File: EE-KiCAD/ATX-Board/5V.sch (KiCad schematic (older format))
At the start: 23 parts, among them Q101 BSC026N08NS5ATMA1, Q102 BSC026N08NS5ATMA1, Q103 BSC026N08NS5ATMA1, Q104 BSC026N08NS5ATMA1, U102 TPS53015

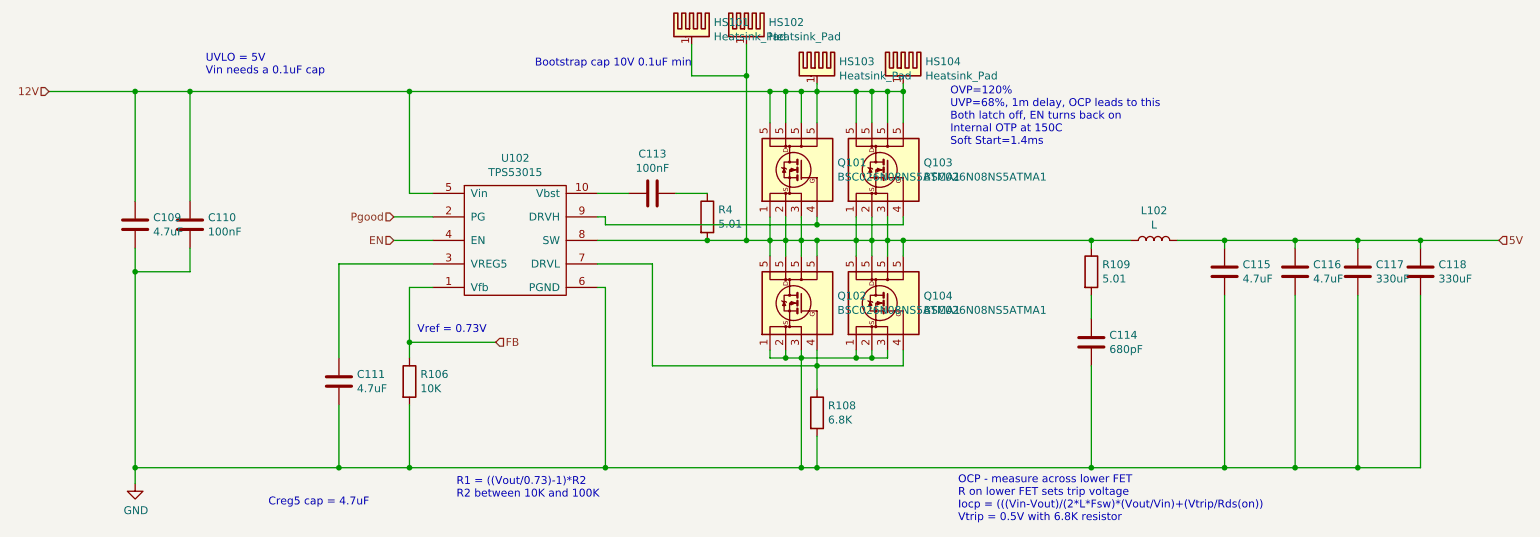
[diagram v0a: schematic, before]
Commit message: Finish first draft of PCBs.  Pulled PCBs into OpenSCAD for fitment.
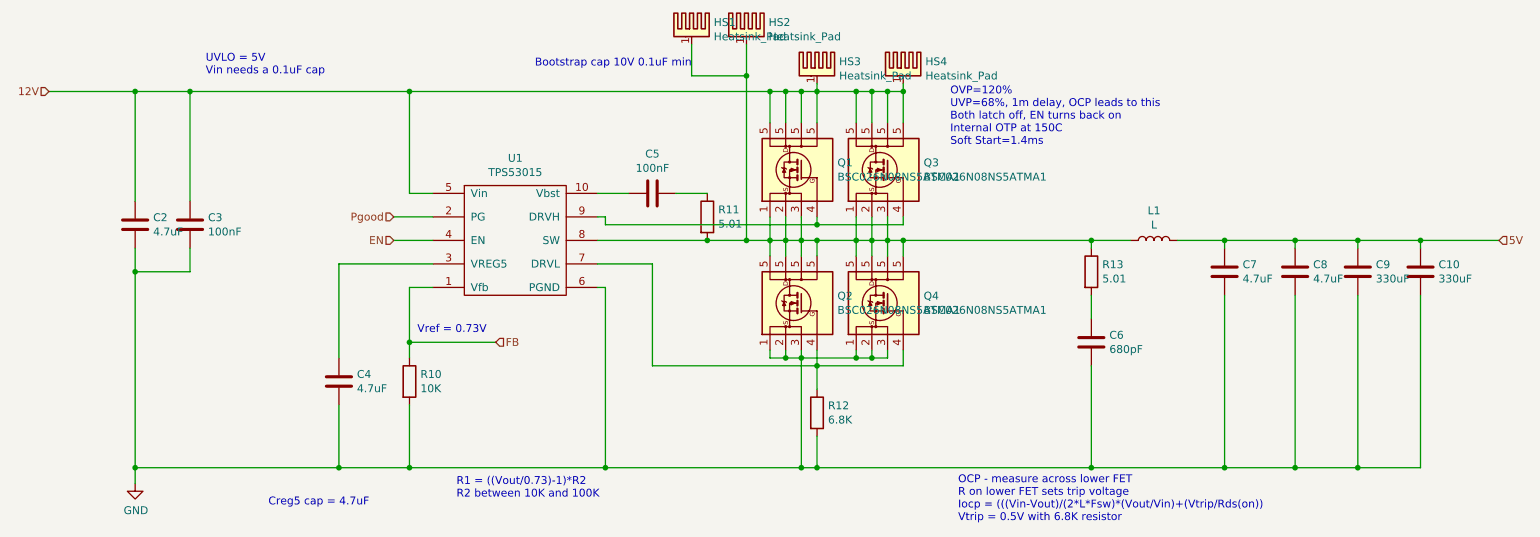
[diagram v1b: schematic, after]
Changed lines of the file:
@@
 $Descr USLedger 17000 11000
 encoding utf-8
-Sheet 6 9
+Sheet 8 8
 Title ""
 Date "2018-08-23"
@@
 AR Path="/5B7F1B83" Ref="U?"  Part="1"
 AR Path="/603813BC/5B7F1B83" Ref="U1"  Part="1"
-F 0 "U102" H 8425 5775 50  0000 C CNN
+F 0 "U1" H 8425 5775 50  0000 C CNN
 F 1 "TPS53015" H 8425 5684 50  0000 C CNN
 F 2 "AEvan:VSSOP-10_2.4x2.1mm_Pitch0.5mm" H 8500 4850 50  0001 C CNN
@@
 AR Path="/5B7EFFE7/5B7F1CF3" Ref="Q101"  Part="1"
 AR Path="/603813BC/5B7F1CF3" Ref="Q1"  Part="1"
-F 0 "Q101" V 10296 4570 50  0000 R CNN
+F 0 "Q1" V 10296 4570 50  0000 R CNN
 F 1 "BSC026N08NS5ATMA1" V 10205 4570 50  0000 R CNN
 F 2 "Package_TO_SOT_SMD:TDSON-8-1" H 10250 5000 50  0001 C CIN
@@
 AR Path="/5B7EFFE7/5B7F1D6B" Ref="Q102"  Part="1"
 AR Path="/603813BC/5B7F1D6B" Ref="Q2"  Part="1"
-F 0 "Q102" V 10296 5420 50  0000 R CNN
+F 0 "Q2" V 10296 5420 50  0000 R CNN
 F 1 "BSC026N08NS5ATMA1" V 10205 5420 50  0000 R CNN
 F 2 "Package_TO_SOT_SMD:TDSON-8-1" H 10250 5850 50  0001 C CIN
@@
 AR Path="/5B7EFFE7/5B7F1E13" Ref="L102"  Part="1"
 AR Path="/603813BC/5B7F1E13" Ref="L1"  Part="1"
-F 0 "L102" V 12690 5250 50  0000 C CNN
+F 0 "L1" V 12690 5250 50  0000 C CNN
 F 1 "L" V 12599 5250 50  0000 C CNN
 F 2 "Inductor_SMD:L_12x12mm_H8mm" H 12500 5250 50  0001 C CNN
@@
 AR Path="/5B7EFFE7/5B7F1F01" Ref="C115"  Part="1"
 AR Path="/603813BC/5B7F1F01" Ref="C7"  Part="1"
-F 0 "C115" H 13065 5496 50  0000 L CNN
+F 0 "C7" H 13065 5496 50  0000 L CNN
 F 1 "4.7uF" H 13065 5405 50  0000 L CNN
 F 2 "AEvan:0805_C" H 12988 5300 50  0001 C CNN
@@
 AR Path="/5B7EFFE7/5B7F1F63" Ref="C116"  Part="1"
 AR Path="/603813BC/5B7F1F63" Ref="C8"  Part="1"
-F 0 "C116" H 13515 5496 50  0000 L CNN
+F 0 "C8" H 13515 5496 50  0000 L CNN
 F 1 "4.7uF" H 13515 5405 50  0000 L CNN
 F 2 "AEvan:0805_C" H 13438 5300 50  0001 C CNN
@@
 AR Path="/5B7EFFE7/5B7F1FA1" Ref="C117"  Part="1"
 AR Path="/603813BC/5B7F1FA1" Ref="C9"  Part="1"
-F 0 "C117" H 13915 5496 50  0000 L CNN
+F 0 "C9" H 13915 5496 50  0000 L CNN
 F 1 "330uF" H 13915 5405 50  0000 L CNN
 F 2 "Capacitor_THT:C_Radial_D6.3mm_H7.0mm_P2.50mm" H 13838 5300 50  0001 C CNN
@@
 AR Path="/5B7EFFE7/5B7F1FD7" Ref="C118"  Part="1"
 AR Path="/603813BC/5B7F1FD7" Ref="C10"  Part="1"
-F 0 "C118" H 14315 5496 50  0000 L CNN
+F 0 "C10" H 14315 5496 50  0000 L CNN
 F 1 "330uF" H 14315 5405 50  0000 L CNN
 F 2 "Capacitor_THT:C_Radial_D6.3mm_H7.0mm_P2.50mm" H 14238 5300 50  0001 C CNN
@@
 AR Path="/5B7EFFE7/5B7F2039" Ref="C113"  Part="1"
 AR Path="/603813BC/5B7F2039" Ref="C5"  Part="1"
-F 0 "C113" V 9048 4950 50  0000 C CNN
+F 0 "C5" V 9048 4950 50  0000 C CNN
 F 1 "100nF" V 9139 4950 50  0000 C CNN
 F 2 "AEvan:0805_C" H 9338 4800 50  0001 C CNN
@@
 AR Path="/5B7EFFE7/5B7F2089" Ref="C114"  Part="1"
 AR Path="/603813BC/5B7F2089" Ref="C6"  Part="1"
-F 0 "C114" H 12215 5946 50  0000 L CNN
+F 0 "C6" H 12215 5946 50  0000 L CNN
 F 1 "680pF" H 12215 5855 50  0000 L CNN
 F 2 "AEvan:0805_C" H 12138 5750 50  0001 C CNN
@@
 AR Path="/5B7EFFE7/5B7F2119" Ref="C111"  Part="1"
 AR Path="/603813BC/5B7F2119" Ref="C4"  Part="1"
-F 0 "C111" H 7415 6196 50  0000 L CNN
+F 0 "C4" H 7415 6196 50  0000 L CNN
 F 1 "4.7uF" H 7415 6105 50  0000 L CNN
 F 2 "AEvan:0805_C" H 7338 6000 50  0001 C CNN
@@
 AR Path="/5B7EFFE7/5B7F2193" Ref="C110"  Part="1"
 AR Path="/603813BC/5B7F2193" Ref="C3"  Part="1"
-F 0 "C110" H 6465 5196 50  0000 L CNN
+F 0 "C3" H 6465 5196 50  0000 L CNN
 F 1 "100nF" H 6465 5105 50  0000 L CNN
 F 2 "AEvan:0805_C" H 6388 5000 50  0001 C CNN
@@
 AR Path="/5B7EFFE7/5B7F21EA" Ref="C109"  Part="1"
 AR Path="/603813BC/5B7F21EA" Ref="C2"  Part="1"
-F 0 "C109" H 6115 5196 50  0000 L CNN
+F 0 "C2" H 6115 5196 50  0000 L CNN
 F 1 "4.7uF" H 6115 5105 50  0000 L CNN
 F 2 "AEvan:0805_C" H 6038 5000 50  0001 C CNN
@@
 AR Path="/5B7EFFE7/5B7F2291" Ref="R108"  Part="1"
 AR Path="/603813BC/5B7F2291" Ref="R12"  Part="1"
-F 0 "R108" H 10420 6396 50  0000 L CNN
+F 0 "R12" H 10420 6396 50  0000 L CNN
 F 1 "6.8K" H 10420 6305 50  0000 L CNN
 F 2 "AEvan:0805_R" V 10280 6350 50  0001 C CNN
@@
 AR Path="/5B7EFFE7/5B7F2363" Ref="R109"  Part="1"
 AR Path="/603813BC/5B7F2363" Ref="R13"  Part="1"
-F 0 "R109" H 12170 5496 50  0000 L CNN
+F 0 "R13" H 12170 5496 50  0000 L CNN
 F 1 "5.01" H 12170 5405 50  0000 L CNN
 F 2 "AEvan:0805_R" V 12030 5450 50  0001 C CNN
@@
 AR Path="/5B7EFFE7/5B7F3FE7" Ref="#PWR0111"  Part="1"
 AR Path="/603813BC/5B7F3FE7" Ref="#PWR01"  Part="1"
-F 0 "#PWR0111" H 6000 6550 50  0001 C CNN
+F 0 "#PWR01" H 6000 6550 50  0001 C CNN
 F 1 "GND" H 6005 6627 50  0000 C CNN
 F 2 "" H 6000 6800 50  0001 C CNN
@@
 AR Path="/5B7EFFE7/5BA7D9F8" Ref="HS103"  Part="1"
 AR Path="/603813BC/5BA7D9F8" Ref="HS3"  Part="1"
-F 0 "HS103" H 10491 4191 50  0000 L CNN
+F 0 "HS3" H 10491 4191 50  0000 L CNN
 F 1 "Heatsink_Pad" H 10491 4100 50  0000 L CNN
 F 2 "AEvan:5X6-HEATSINK" H 10362 4100 50  0001 C CNN
@@
 AR Path="/5B7EFFE7/5BA7DAB4" Ref="HS102"  Part="1"
 AR Path="/603813BC/5BA7DAB4" Ref="HS2"  Part="1"
-F 0 "HS102" H 10041 3941 50  0000 L CNN
+F 0 "HS2" H 10041 3941 50  0000 L CNN
 F 1 "Heatsink_Pad" H 10041 3850 50  0000 L CNN
 F 2 "AEvan:5X6-HEATSINK" H 9912 3850 50  0001 C CNN
@@
 AR Path="/5B7EFFE7/5BFFF423" Ref="Q103"  Part="1"
 AR Path="/603813BC/5BFFF423" Ref="Q3"  Part="1"
-F 0 "Q103" V 10846 4570 50  0000 R CNN
+F 0 "Q3" V 10846 4570 50  0000 R CNN
 F 1 "BSC026N08NS5ATMA1" V 10755 4570 50  0000 R CNN
 F 2 "Package_TO_SOT_SMD:TDSON-8-1" H 10800 5000 50  0001 C CIN
@@
 AR Path="/5B7EFFE7/5BFFF47F" Ref="Q104"  Part="1"
 AR Path="/603813BC/5BFFF47F" Ref="Q4"  Part="1"
-F 0 "Q104" V 10846 5420 50  0000 R CNN
+F 0 "Q4" V 10846 5420 50  0000 R CNN
 F 1 "BSC026N08NS5ATMA1" V 10755 5420 50  0000 R CNN
 F 2 "Package_TO_SOT_SMD:TDSON-8-1" H 10800 5850 50  0001 C CIN
@@
 AR Path="/5B7EFFE7/5BFEAE61" Ref="HS101"  Part="1"
 AR Path="/603813BC/5BFEAE61" Ref="HS1"  Part="1"
-F 0 "HS101" H 9691 3941 50  0000 L CNN
+F 0 "HS1" H 9691 3941 50  0000 L CNN
 F 1 "Heatsink_Pad" H 9691 3850 50  0000 L CNN
 F 2 "AEvan:5X6-HEATSINK" H 9562 3850 50  0001 C CNN
@@
 AR Path="/5B7EFFE7/5BFEAEAD" Ref="HS104"  Part="1"
 AR Path="/603813BC/5BFEAEAD" Ref="HS4"  Part="1"
-F 0 "HS104" H 11041 4191 50  0000 L CNN
+F 0 "HS4" H 11041 4191 50  0000 L CNN
 F 1 "Heatsink_Pad" H 11041 4100 50  0000 L CNN
 F 2 "AEvan:5X6-HEATSINK" H 10912 4100 50  0001 C CNN
@@
 AR Path="/5B7EFFE7/6033D936" Ref="R4"  Part="1"
 AR Path="/603813BC/6033D936" Ref="R11"  Part="1"
-F 0 "R4" H 9720 5146 50  0000 L CNN
+F 0 "R11" H 9720 5146 50  0000 L CNN
 F 1 "5.01" H 9720 5055 50  0000 L CNN
 F 2 "AEvan:0805_R" V 9580 5100 50  0001 C CNN
@@
 AR Path="/5B7EFFE7/5B7F23DB" Ref="R106"  Part="1"
 AR Path="/603813BC/5B7F23DB" Ref="R10"  Part="1"
-F 0 "R106" H 7820 6196 50  0000 L CNN
+F 0 "R10" H 7820 6196 50  0000 L CNN
 F 1 "10K" H 7820 6105 50  0000 L CNN
 F 2 "AEvan:0805_R" V 7680 6150 50  0001 C CNN

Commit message: add tabs on PCBs to set where they are in the box.  Box adjustments.
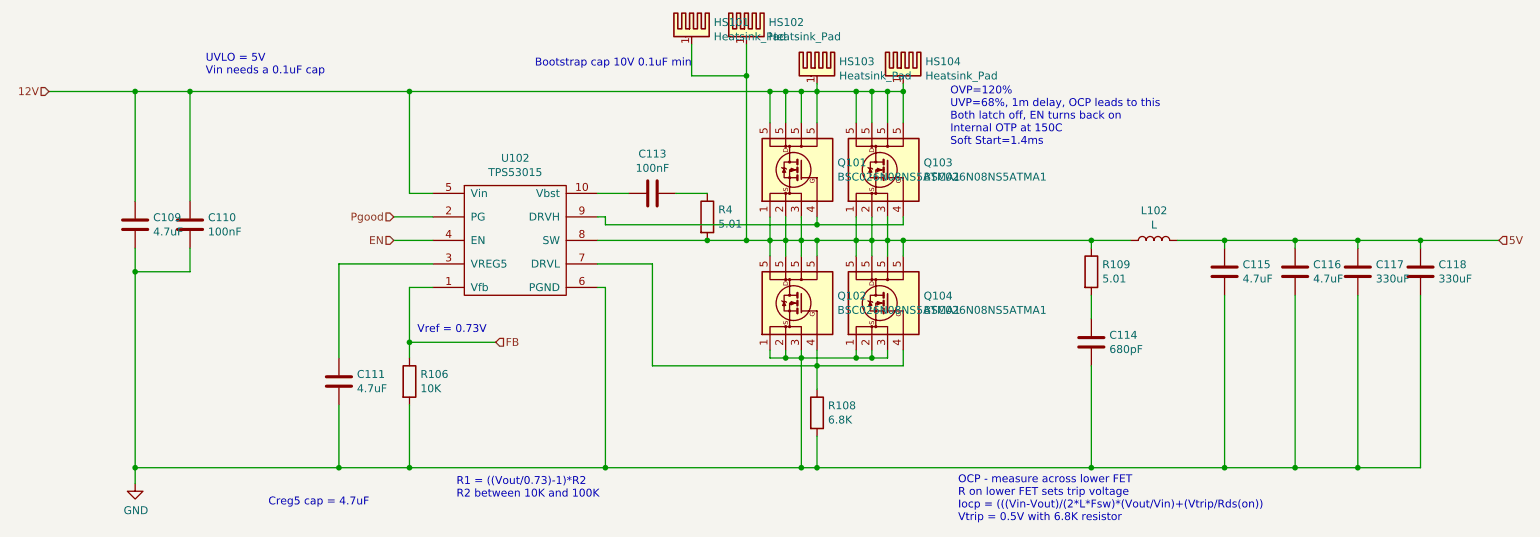
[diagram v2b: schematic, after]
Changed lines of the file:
@@
 $Descr USLedger 17000 11000
 encoding utf-8
-Sheet 8 8
+Sheet 6 8
 Title ""
 Date "2018-08-23"
@@
 AR Path="/5B7F1B83" Ref="U?"  Part="1"
 AR Path="/603813BC/5B7F1B83" Ref="U1"  Part="1"
-F 0 "U1" H 8425 5775 50  0000 C CNN
+F 0 "U102" H 8425 5775 50  0000 C CNN
 F 1 "TPS53015" H 8425 5684 50  0000 C CNN
 F 2 "AEvan:VSSOP-10_2.4x2.1mm_Pitch0.5mm" H 8500 4850 50  0001 C CNN
@@
 AR Path="/5B7EFFE7/5B7F1CF3" Ref="Q101"  Part="1"
 AR Path="/603813BC/5B7F1CF3" Ref="Q1"  Part="1"
-F 0 "Q1" V 10296 4570 50  0000 R CNN
+F 0 "Q101" V 10296 4570 50  0000 R CNN
 F 1 "BSC026N08NS5ATMA1" V 10205 4570 50  0000 R CNN
 F 2 "Package_TO_SOT_SMD:TDSON-8-1" H 10250 5000 50  0001 C CIN
@@
 AR Path="/5B7EFFE7/5B7F1D6B" Ref="Q102"  Part="1"
 AR Path="/603813BC/5B7F1D6B" Ref="Q2"  Part="1"
-F 0 "Q2" V 10296 5420 50  0000 R CNN
+F 0 "Q102" V 10296 5420 50  0000 R CNN
 F 1 "BSC026N08NS5ATMA1" V 10205 5420 50  0000 R CNN
 F 2 "Package_TO_SOT_SMD:TDSON-8-1" H 10250 5850 50  0001 C CIN
@@
 AR Path="/5B7EFFE7/5B7F1E13" Ref="L102"  Part="1"
 AR Path="/603813BC/5B7F1E13" Ref="L1"  Part="1"
-F 0 "L1" V 12690 5250 50  0000 C CNN
+F 0 "L102" V 12690 5250 50  0000 C CNN
 F 1 "L" V 12599 5250 50  0000 C CNN
 F 2 "Inductor_SMD:L_12x12mm_H8mm" H 12500 5250 50  0001 C CNN
@@
 AR Path="/5B7EFFE7/5B7F1F01" Ref="C115"  Part="1"
 AR Path="/603813BC/5B7F1F01" Ref="C7"  Part="1"
-F 0 "C7" H 13065 5496 50  0000 L CNN
+F 0 "C115" H 13065 5496 50  0000 L CNN
 F 1 "4.7uF" H 13065 5405 50  0000 L CNN
 F 2 "AEvan:0805_C" H 12988 5300 50  0001 C CNN
@@
 AR Path="/5B7EFFE7/5B7F1F63" Ref="C116"  Part="1"
 AR Path="/603813BC/5B7F1F63" Ref="C8"  Part="1"
-F 0 "C8" H 13515 5496 50  0000 L CNN
+F 0 "C116" H 13515 5496 50  0000 L CNN
 F 1 "4.7uF" H 13515 5405 50  0000 L CNN
 F 2 "AEvan:0805_C" H 13438 5300 50  0001 C CNN
@@
 AR Path="/5B7EFFE7/5B7F1FA1" Ref="C117"  Part="1"
 AR Path="/603813BC/5B7F1FA1" Ref="C9"  Part="1"
-F 0 "C9" H 13915 5496 50  0000 L CNN
+F 0 "C117" H 13915 5496 50  0000 L CNN
 F 1 "330uF" H 13915 5405 50  0000 L CNN
 F 2 "Capacitor_THT:C_Radial_D6.3mm_H7.0mm_P2.50mm" H 13838 5300 50  0001 C CNN
@@
 AR Path="/5B7EFFE7/5B7F1FD7" Ref="C118"  Part="1"
 AR Path="/603813BC/5B7F1FD7" Ref="C10"  Part="1"
-F 0 "C10" H 14315 5496 50  0000 L CNN
+F 0 "C118" H 14315 5496 50  0000 L CNN
 F 1 "330uF" H 14315 5405 50  0000 L CNN
 F 2 "Capacitor_THT:C_Radial_D6.3mm_H7.0mm_P2.50mm" H 14238 5300 50  0001 C CNN
@@
 AR Path="/5B7EFFE7/5B7F2039" Ref="C113"  Part="1"
 AR Path="/603813BC/5B7F2039" Ref="C5"  Part="1"
-F 0 "C5" V 9048 4950 50  0000 C CNN
+F 0 "C113" V 9048 4950 50  0000 C CNN
 F 1 "100nF" V 9139 4950 50  0000 C CNN
 F 2 "AEvan:0805_C" H 9338 4800 50  0001 C CNN
@@
 AR Path="/5B7EFFE7/5B7F2089" Ref="C114"  Part="1"
 AR Path="/603813BC/5B7F2089" Ref="C6"  Part="1"
-F 0 "C6" H 12215 5946 50  0000 L CNN
+F 0 "C114" H 12215 5946 50  0000 L CNN
 F 1 "680pF" H 12215 5855 50  0000 L CNN
 F 2 "AEvan:0805_C" H 12138 5750 50  0001 C CNN
@@
 AR Path="/5B7EFFE7/5B7F2119" Ref="C111"  Part="1"
 AR Path="/603813BC/5B7F2119" Ref="C4"  Part="1"
-F 0 "C4" H 7415 6196 50  0000 L CNN
+F 0 "C111" H 7415 6196 50  0000 L CNN
 F 1 "4.7uF" H 7415 6105 50  0000 L CNN
 F 2 "AEvan:0805_C" H 7338 6000 50  0001 C CNN
@@
 AR Path="/5B7EFFE7/5B7F2193" Ref="C110"  Part="1"
 AR Path="/603813BC/5B7F2193" Ref="C3"  Part="1"
-F 0 "C3" H 6465 5196 50  0000 L CNN
+F 0 "C110" H 6465 5196 50  0000 L CNN
 F 1 "100nF" H 6465 5105 50  0000 L CNN
 F 2 "AEvan:0805_C" H 6388 5000 50  0001 C CNN
@@
 AR Path="/5B7EFFE7/5B7F21EA" Ref="C109"  Part="1"
 AR Path="/603813BC/5B7F21EA" Ref="C2"  Part="1"
-F 0 "C2" H 6115 5196 50  0000 L CNN
+F 0 "C109" H 6115 5196 50  0000 L CNN
 F 1 "4.7uF" H 6115 5105 50  0000 L CNN
 F 2 "AEvan:0805_C" H 6038 5000 50  0001 C CNN
@@
 AR Path="/5B7EFFE7/5B7F2291" Ref="R108"  Part="1"
 AR Path="/603813BC/5B7F2291" Ref="R12"  Part="1"
-F 0 "R12" H 10420 6396 50  0000 L CNN
+F 0 "R108" H 10420 6396 50  0000 L CNN
 F 1 "6.8K" H 10420 6305 50  0000 L CNN
 F 2 "AEvan:0805_R" V 10280 6350 50  0001 C CNN
@@
 AR Path="/5B7EFFE7/5B7F2363" Ref="R109"  Part="1"
 AR Path="/603813BC/5B7F2363" Ref="R13"  Part="1"
-F 0 "R13" H 12170 5496 50  0000 L CNN
+F 0 "R109" H 12170 5496 50  0000 L CNN
 F 1 "5.01" H 12170 5405 50  0000 L CNN
 F 2 "AEvan:0805_R" V 12030 5450 50  0001 C CNN
@@
 AR Path="/5B7EFFE7/5B7F3FE7" Ref="#PWR0111"  Part="1"
 AR Path="/603813BC/5B7F3FE7" Ref="#PWR01"  Part="1"
-F 0 "#PWR01" H 6000 6550 50  0001 C CNN
+F 0 "#PWR0111" H 6000 6550 50  0001 C CNN
 F 1 "GND" H 6005 6627 50  0000 C CNN
 F 2 "" H 6000 6800 50  0001 C CNN
@@
 AR Path="/5B7EFFE7/5BA7D9F8" Ref="HS103"  Part="1"
 AR Path="/603813BC/5BA7D9F8" Ref="HS3"  Part="1"
-F 0 "HS3" H 10491 4191 50  0000 L CNN
+F 0 "HS103" H 10491 4191 50  0000 L CNN
 F 1 "Heatsink_Pad" H 10491 4100 50  0000 L CNN
 F 2 "AEvan:5X6-HEATSINK" H 10362 4100 50  0001 C CNN
@@
 AR Path="/5B7EFFE7/5BA7DAB4" Ref="HS102"  Part="1"
 AR Path="/603813BC/5BA7DAB4" Ref="HS2"  Part="1"
-F 0 "HS2" H 10041 3941 50  0000 L CNN
+F 0 "HS102" H 10041 3941 50  0000 L CNN
 F 1 "Heatsink_Pad" H 10041 3850 50  0000 L CNN
 F 2 "AEvan:5X6-HEATSINK" H 9912 3850 50  0001 C CNN
@@
 AR Path="/5B7EFFE7/5BFFF423" Ref="Q103"  Part="1"
 AR Path="/603813BC/5BFFF423" Ref="Q3"  Part="1"
-F 0 "Q3" V 10846 4570 50  0000 R CNN
+F 0 "Q103" V 10846 4570 50  0000 R CNN
 F 1 "BSC026N08NS5ATMA1" V 10755 4570 50  0000 R CNN
 F 2 "Package_TO_SOT_SMD:TDSON-8-1" H 10800 5000 50  0001 C CIN
@@
 AR Path="/5B7EFFE7/5BFFF47F" Ref="Q104"  Part="1"
 AR Path="/603813BC/5BFFF47F" Ref="Q4"  Part="1"
-F 0 "Q4" V 10846 5420 50  0000 R CNN
+F 0 "Q104" V 10846 5420 50  0000 R CNN
 F 1 "BSC026N08NS5ATMA1" V 10755 5420 50  0000 R CNN
 F 2 "Package_TO_SOT_SMD:TDSON-8-1" H 10800 5850 50  0001 C CIN
@@
 AR Path="/5B7EFFE7/5BFEAE61" Ref="HS101"  Part="1"
 AR Path="/603813BC/5BFEAE61" Ref="HS1"  Part="1"
-F 0 "HS1" H 9691 3941 50  0000 L CNN
+F 0 "HS101" H 9691 3941 50  0000 L CNN
 F 1 "Heatsink_Pad" H 9691 3850 50  0000 L CNN
 F 2 "AEvan:5X6-HEATSINK" H 9562 3850 50  0001 C CNN
@@
 AR Path="/5B7EFFE7/5BFEAEAD" Ref="HS104"  Part="1"
 AR Path="/603813BC/5BFEAEAD" Ref="HS4"  Part="1"
-F 0 "HS4" H 11041 4191 50  0000 L CNN
+F 0 "HS104" H 11041 4191 50  0000 L CNN
 F 1 "Heatsink_Pad" H 11041 4100 50  0000 L CNN
 F 2 "AEvan:5X6-HEATSINK" H 10912 4100 50  0001 C CNN
@@
 AR Path="/5B7EFFE7/6033D936" Ref="R4"  Part="1"
 AR Path="/603813BC/6033D936" Ref="R11"  Part="1"
-F 0 "R11" H 9720 5146 50  0000 L CNN
+F 0 "R4" H 9720 5146 50  0000 L CNN
 F 1 "5.01" H 9720 5055 50  0000 L CNN
 F 2 "AEvan:0805_R" V 9580 5100 50  0001 C CNN
@@
 AR Path="/5B7EFFE7/5B7F23DB" Ref="R106"  Part="1"
 AR Path="/603813BC/5B7F23DB" Ref="R10"  Part="1"
-F 0 "R10" H 7820 6196 50  0000 L CNN
+F 0 "R106" H 7820 6196 50  0000 L CNN
 F 1 "10K" H 7820 6105 50  0000 L CNN
 F 2 "AEvan:0805_R" V 7680 6150 50  0001 C CNN
